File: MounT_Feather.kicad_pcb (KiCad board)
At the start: 2 copper layers, 50.8 x 22.9 mm, 11 parts, among them J1 Adafruit_Feather_stagger, J2 DB25_Male, U1 MAX3232

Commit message: remove unused models, update readme
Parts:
- J1: value Adafruit_Feather_stagger -> Adafruit_Feather
- S1: footprint 0_LOCAL:SW_DS04-254-1L-01BK -> 0_LOCAL:CSS-121xC; moved to F.Cu
- moved S1 8.95 mm to (168.9, 96.5), turned to 90 degrees
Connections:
- net /CTS renamed /CTS_232
- net /DCD renamed /DCD_232
- net /DSR renamed /DSR_232
- net /DTR renamed /DTR_232
- net /RTS renamed /RTS_232
- net /RXD renamed /RX_232
- net /RXD_TTL renamed /RX_TTL
- net /TXD renamed /TX_232
- net /TXD_TTL renamed /TX_TTL
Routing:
- net /En: track 26.7 -> 19.7 mm
- net /RX_TTL: track 18.0 -> 18.7 mm
- net /TX_TTL: track 19.2 -> 19.9 mm
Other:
- board text added: "Feather"
- board text added: "MounT"

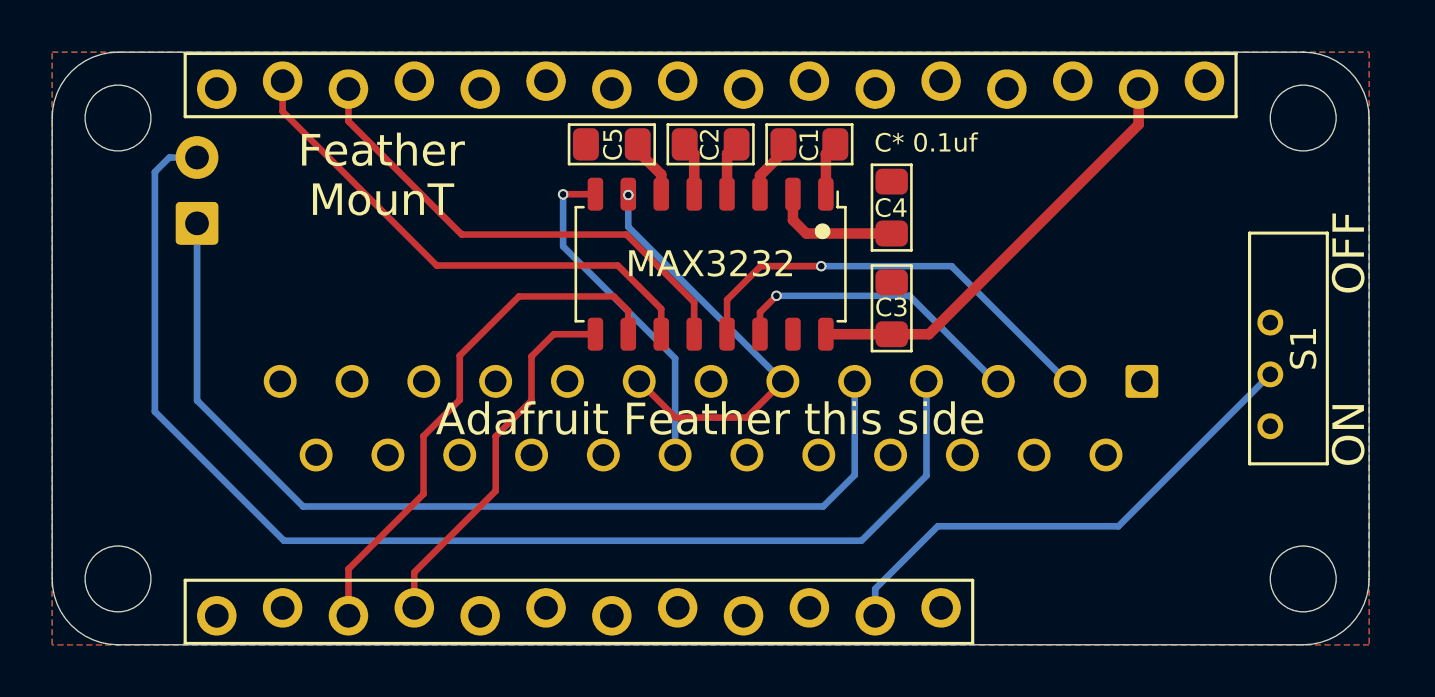
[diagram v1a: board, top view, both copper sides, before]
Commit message: reduce pin stagger offset from 12 mils to 8 mils
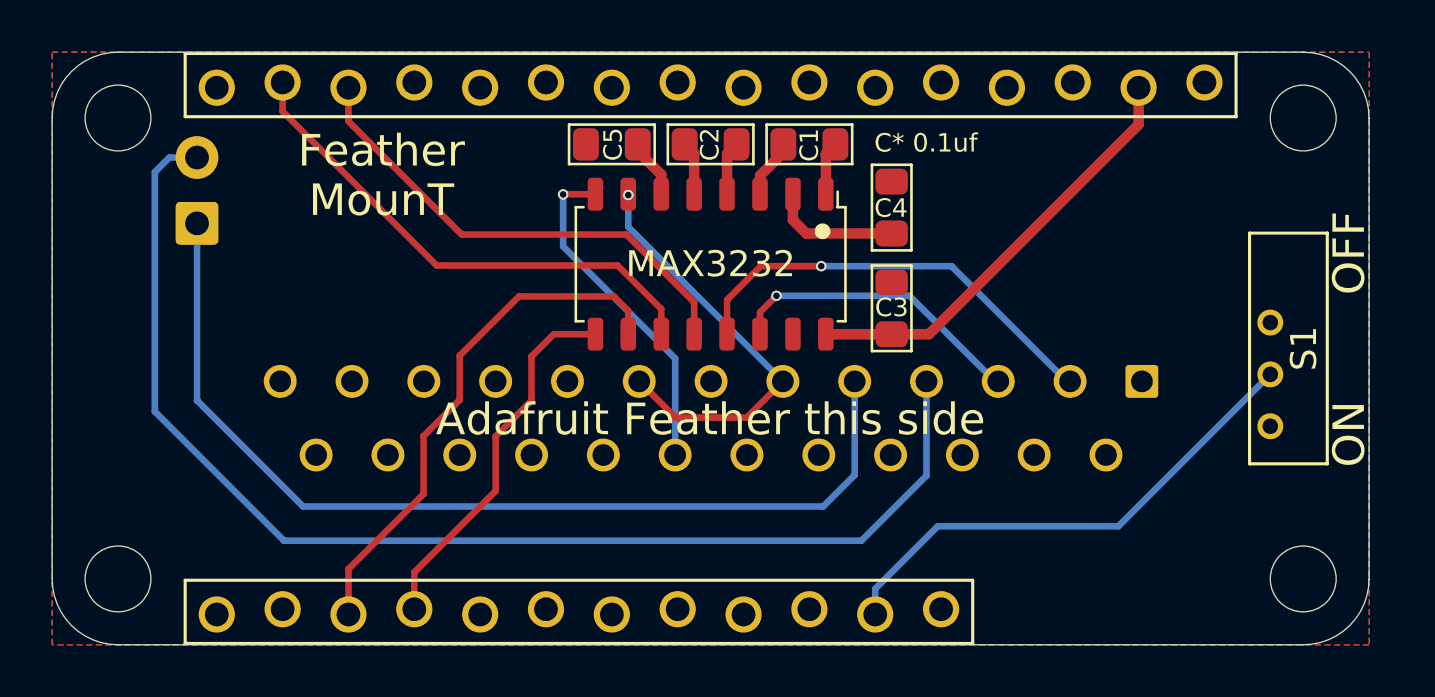
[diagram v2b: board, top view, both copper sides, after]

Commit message: reduce pin stagger offset to 4mil
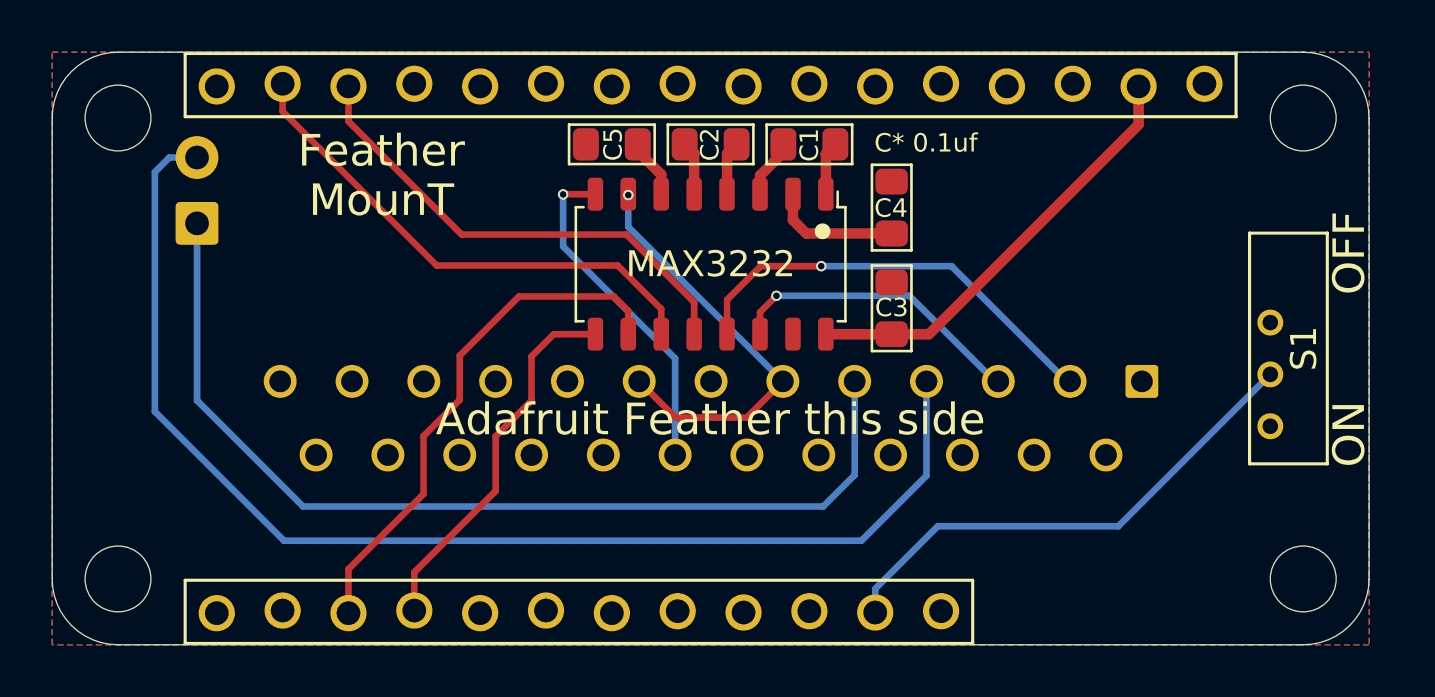
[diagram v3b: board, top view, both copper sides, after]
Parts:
- J1: footprint 0_LOCAL:Adafruit_Feather_stagger -> 0_LOCAL:Adafruit_Feather_stagger_4mil
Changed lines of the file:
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@@
     (add_net "Net-(C5-Pad1)")
   )
-  (module 0_LOCAL:Adafruit_Feather_stagger (layer F.Cu)
+  (module 0_LOCAL:Adafruit_Feather_stagger_4mil (layer F.Cu)
     (at 147.32 96.52 180)
     (fp_text reference J1 (at -5.842 0) (layer F.SilkS) hide
@@
     (pad "" np_thru_hole circle (at -22.86 8.89 180) (size 2.54 2.54) (drill 2.54) (layers *.Cu *.Mask))
     (pad "" np_thru_hole circle (at -22.86 -8.89 180) (size 2.54 2.54) (drill 2.54) (layers *.Cu *.Mask))
-    (pad 16 thru_hole circle (at 19.05 10.0584 180) (size 1.397 1.397) (drill 0.9144) (layers *.Cu *.Mask)
+    (pad 16 thru_hole circle (at 19.05 10.1092 180) (size 1.397 1.397) (drill 0.9144) (layers *.Cu *.Mask)
       (net 1 GND))
-    (pad 15 thru_hole circle (at 16.51 10.2616 180) (size 1.397 1.397) (drill 0.9144) (layers *.Cu *.Mask)
+    (pad 15 thru_hole circle (at 16.51 10.2108 180) (size 1.397 1.397) (drill 0.9144) (layers *.Cu *.Mask)
       (net 12 /TX_TTL))
-    (pad 14 thru_hole circle (at 13.97 10.0584 180) (size 1.397 1.397) (drill 0.9144) (layers *.Cu *.Mask)
+    (pad 14 thru_hole circle (at 13.97 10.1092 180) (size 1.397 1.397) (drill 0.9144) (layers *.Cu *.Mask)
       (net 13 /RX_TTL))
-    (pad 13 thru_hole circle (at 11.43 10.2616 180) (size 1.397 1.397) (drill 0.9144) (layers *.Cu *.Mask))
-    (pad 12 thru_hole circle (at 8.89 10.0584 180) (size 1.397 1.397) (drill 0.9144) (layers *.Cu *.Mask))
-    (pad 11 thru_hole circle (at 6.35 10.2616 180) (size 1.397 1.397) (drill 0.9144) (layers *.Cu *.Mask))
-    (pad 10 thru_hole circle (at 3.81 10.0584 180) (size 1.397 1.397) (drill 0.9144) (layers *.Cu *.Mask))
-    (pad 9 thru_hole circle (at 1.27 10.2616 180) (size 1.397 1.397) (drill 0.9144) (layers *.Cu *.Mask))
-    (pad 8 thru_hole circle (at -1.27 10.0584 180) (size 1.397 1.397) (drill 0.9144) (layers *.Cu *.Mask))
-    (pad 7 thru_hole circle (at -3.81 10.2616 180) (size 1.397 1.397) (drill 0.9144) (layers *.Cu *.Mask))
-    (pad 6 thru_hole circle (at -6.35 10.0584 180) (size 1.397 1.397) (drill 0.9144) (layers *.Cu *.Mask))
-    (pad 5 thru_hole circle (at -8.89 10.2616 180) (size 1.397 1.397) (drill 0.9144) (layers *.Cu *.Mask))
-    (pad 4 thru_hole circle (at -11.43 10.0584 180) (size 1.397 1.397) (drill 0.9144) (layers *.Cu *.Mask)
+    (pad 13 thru_hole circle (at 11.43 10.2108 180) (size 1.397 1.397) (drill 0.9144) (layers *.Cu *.Mask))
+    (pad 12 thru_hole circle (at 8.89 10.1092 180) (size 1.397 1.397) (drill 0.9144) (layers *.Cu *.Mask))
+    (pad 11 thru_hole circle (at 6.35 10.2108 180) (size 1.397 1.397) (drill 0.9144) (layers *.Cu *.Mask))
+    (pad 10 thru_hole circle (at 3.81 10.1092 180) (size 1.397 1.397) (drill 0.9144) (layers *.Cu *.Mask))
+    (pad 9 thru_hole circle (at 1.27 10.2108 180) (size 1.397 1.397) (drill 0.9144) (layers *.Cu *.Mask))
+    (pad 8 thru_hole circle (at -1.27 10.1092 180) (size 1.397 1.397) (drill 0.9144) (layers *.Cu *.Mask))
+    (pad 7 thru_hole circle (at -3.81 10.2108 180) (size 1.397 1.397) (drill 0.9144) (layers *.Cu *.Mask))
+    (pad 6 thru_hole circle (at -6.35 10.1092 180) (size 1.397 1.397) (drill 0.9144) (layers *.Cu *.Mask))
+    (pad 5 thru_hole circle (at -8.89 10.2108 180) (size 1.397 1.397) (drill 0.9144) (layers *.Cu *.Mask))
+    (pad 4 thru_hole circle (at -11.43 10.1092 180) (size 1.397 1.397) (drill 0.9144) (layers *.Cu *.Mask)
       (net 1 GND))
-    (pad 3 thru_hole circle (at -13.97 10.2616 180) (size 1.397 1.397) (drill 0.9144) (layers *.Cu *.Mask))
-    (pad 2 thru_hole circle (at -16.51 10.0584 180) (size 1.397 1.397) (drill 0.9144) (layers *.Cu *.Mask)
+    (pad 3 thru_hole circle (at -13.97 10.2108 180) (size 1.397 1.397) (drill 0.9144) (layers *.Cu *.Mask))
+    (pad 2 thru_hole circle (at -16.51 10.1092 180) (size 1.397 1.397) (drill 0.9144) (layers *.Cu *.Mask)
       (net 9 +3V3))
-    (pad 1 thru_hole circle (at -19.05 10.2616 180) (size 1.397 1.397) (drill 0.9144) (layers *.Cu *.Mask))
-    (pad 17 thru_hole circle (at 19.05 -10.2616 180) (size 1.397 1.397) (drill 0.9144) (layers *.Cu *.Mask))
-    (pad 18 thru_hole circle (at 16.51 -10.0584 180) (size 1.397 1.397) (drill 0.9144) (layers *.Cu *.Mask))
-    (pad 19 thru_hole circle (at 13.97 -10.2616 180) (size 1.397 1.397) (drill 0.9144) (layers *.Cu *.Mask)
+    (pad 1 thru_hole circle (at -19.05 10.2108 180) (size 1.397 1.397) (drill 0.9144) (layers *.Cu *.Mask))
+    (pad 17 thru_hole circle (at 19.05 -10.2108 180) (size 1.397 1.397) (drill 0.9144) (layers *.Cu *.Mask))
+    (pad 18 thru_hole circle (at 16.51 -10.1092 180) (size 1.397 1.397) (drill 0.9144) (layers *.Cu *.Mask))
+    (pad 19 thru_hole circle (at 13.97 -10.2108 180) (size 1.397 1.397) (drill 0.9144) (layers *.Cu *.Mask)
       (net 10 /DTR_TTL))
-    (pad 20 thru_hole circle (at 11.43 -10.0584 180) (size 1.397 1.397) (drill 0.9144) (layers *.Cu *.Mask)
+    (pad 20 thru_hole circle (at 11.43 -10.1092 180) (size 1.397 1.397) (drill 0.9144) (layers *.Cu *.Mask)
       (net 11 /DSR_TTL))
-    (pad 21 thru_hole circle (at 8.89 -10.2616 180) (size 1.397 1.397) (drill 0.9144) (layers *.Cu *.Mask))
-    (pad 22 thru_hole circle (at 6.35 -10.0584 180) (size 1.397 1.397) (drill 0.9144) (layers *.Cu *.Mask))
-    (pad 23 thru_hole circle (at 3.81 -10.2616 180) (size 1.397 1.397) (drill 0.9144) (layers *.Cu *.Mask))
-    (pad 24 thru_hole circle (at 1.27 -10.0584 180) (size 1.397 1.397) (drill 0.9144) (layers *.Cu *.Mask))
-    (pad 25 thru_hole circle (at -1.27 -10.2616 180) (size 1.397 1.397) (drill 0.9144) (layers *.Cu *.Mask))
-    (pad 26 thru_hole circle (at -3.81 -10.0584 180) (size 1.397 1.397) (drill 0.9144) (layers *.Cu *.Mask))
-    (pad 27 thru_hole circle (at -6.35 -10.2616 180) (size 1.397 1.397) (drill 0.9144) (layers *.Cu *.Mask)
+    (pad 21 thru_hole circle (at 8.89 -10.2108 180) (size 1.397 1.397) (drill 0.9144) (layers *.Cu *.Mask))
+    (pad 22 thru_hole circle (at 6.35 -10.1092 180) (size 1.397 1.397) (drill 0.9144) (layers *.Cu *.Mask))
+    (pad 23 thru_hole circle (at 3.81 -10.2108 180) (size 1.397 1.397) (drill 0.9144) (layers *.Cu *.Mask))
+    (pad 24 thru_hole circle (at 1.27 -10.1346 180) (size 1.397 1.397) (drill 0.9144) (layers *.Cu *.Mask))
+    (pad 25 thru_hole circle (at -1.27 -10.1854 180) (size 1.397 1.397) (drill 0.9144) (layers *.Cu *.Mask))
+    (pad 26 thru_hole circle (at -3.81 -10.1346 180) (size 1.397 1.397) (drill 0.9144) (layers *.Cu *.Mask))
+    (pad 27 thru_hole circle (at -6.35 -10.1854 180) (size 1.397 1.397) (drill 0.9144) (layers *.Cu *.Mask)
       (net 8 /En))
-    (pad 28 thru_hole circle (at -8.89 -10.0584 180) (size 1.397 1.397) (drill 0.9144) (layers *.Cu *.Mask))
+    (pad 28 thru_hole circle (at -8.89 -10.1346 180) (size 1.397 1.397) (drill 0.9144) (layers *.Cu *.Mask))
   )
   (module 0_LOCAL:CSS-121xC (layer F.Cu)

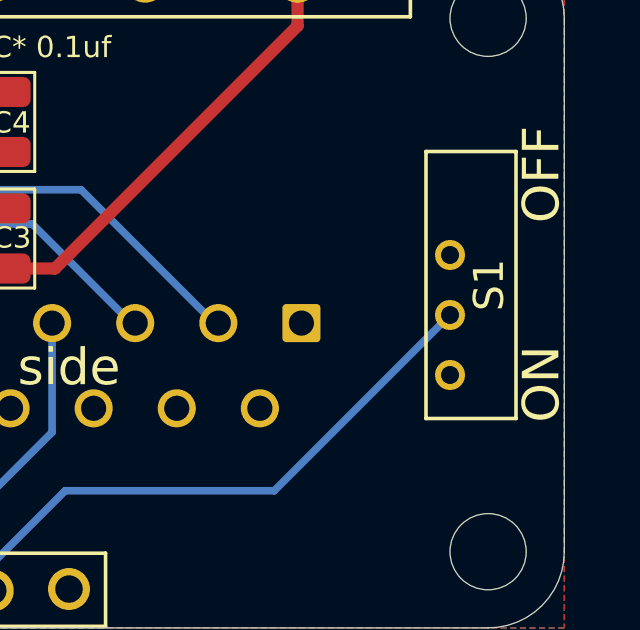
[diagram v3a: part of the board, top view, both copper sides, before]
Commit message: WP2 & Z88, move DE9 shell away from pins. Increase solder pads in S1.
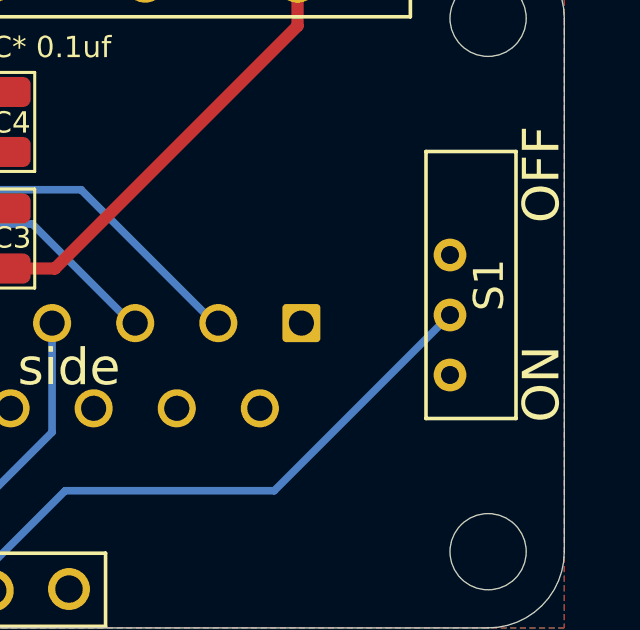
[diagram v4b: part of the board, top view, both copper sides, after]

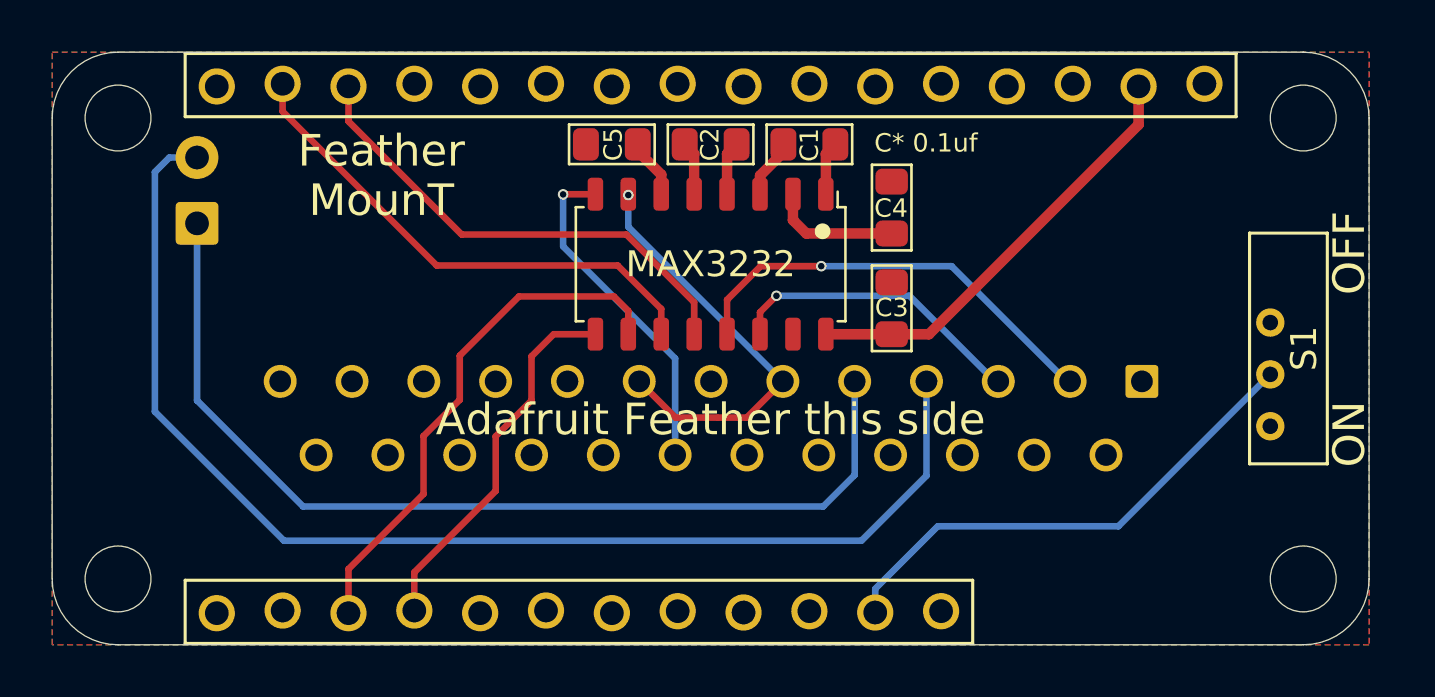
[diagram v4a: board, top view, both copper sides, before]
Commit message: use 6mil stagger, 4mil wasn't good enough
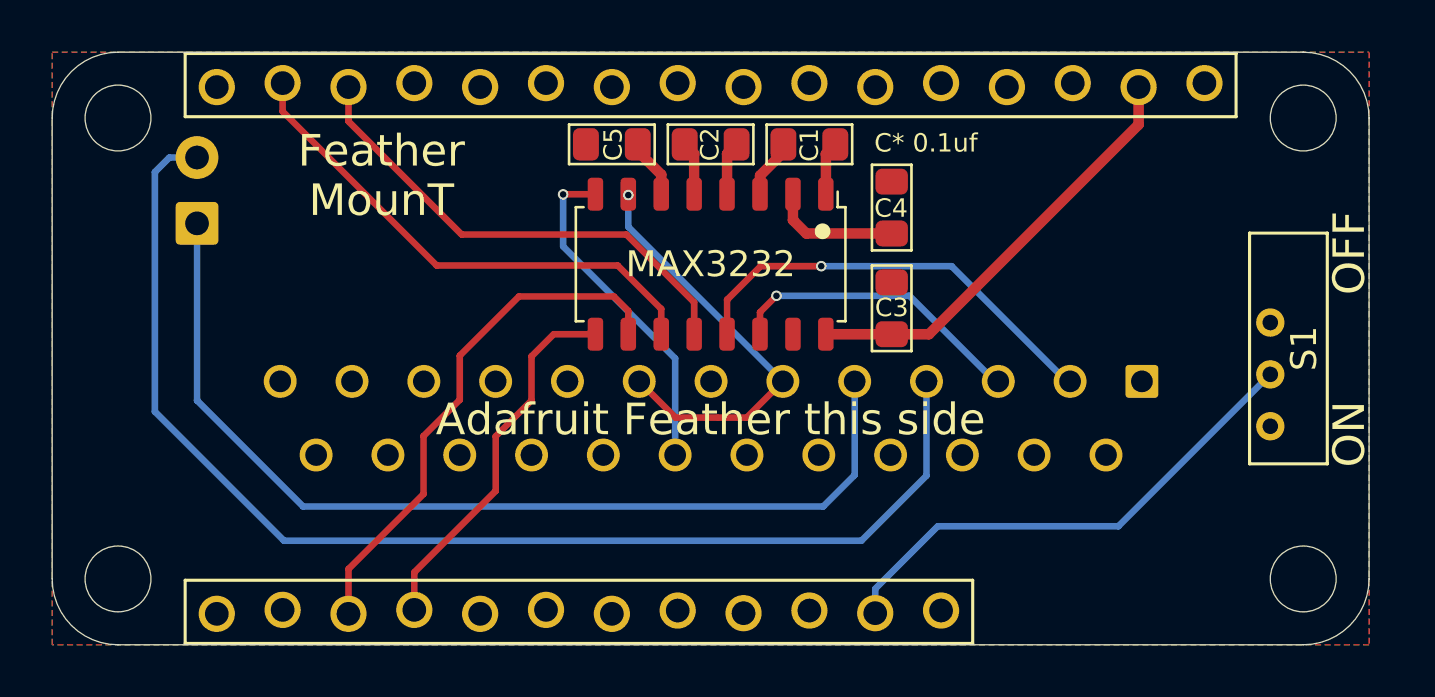
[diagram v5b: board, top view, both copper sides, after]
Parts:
- J1: footprint 0_LOCAL:Adafruit_Feather_stagger_4mil -> 0_LOCAL:Adafruit_Feather_stagger_6mil
